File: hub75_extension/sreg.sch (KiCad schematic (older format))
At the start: 10 parts, among them U1 74HC595

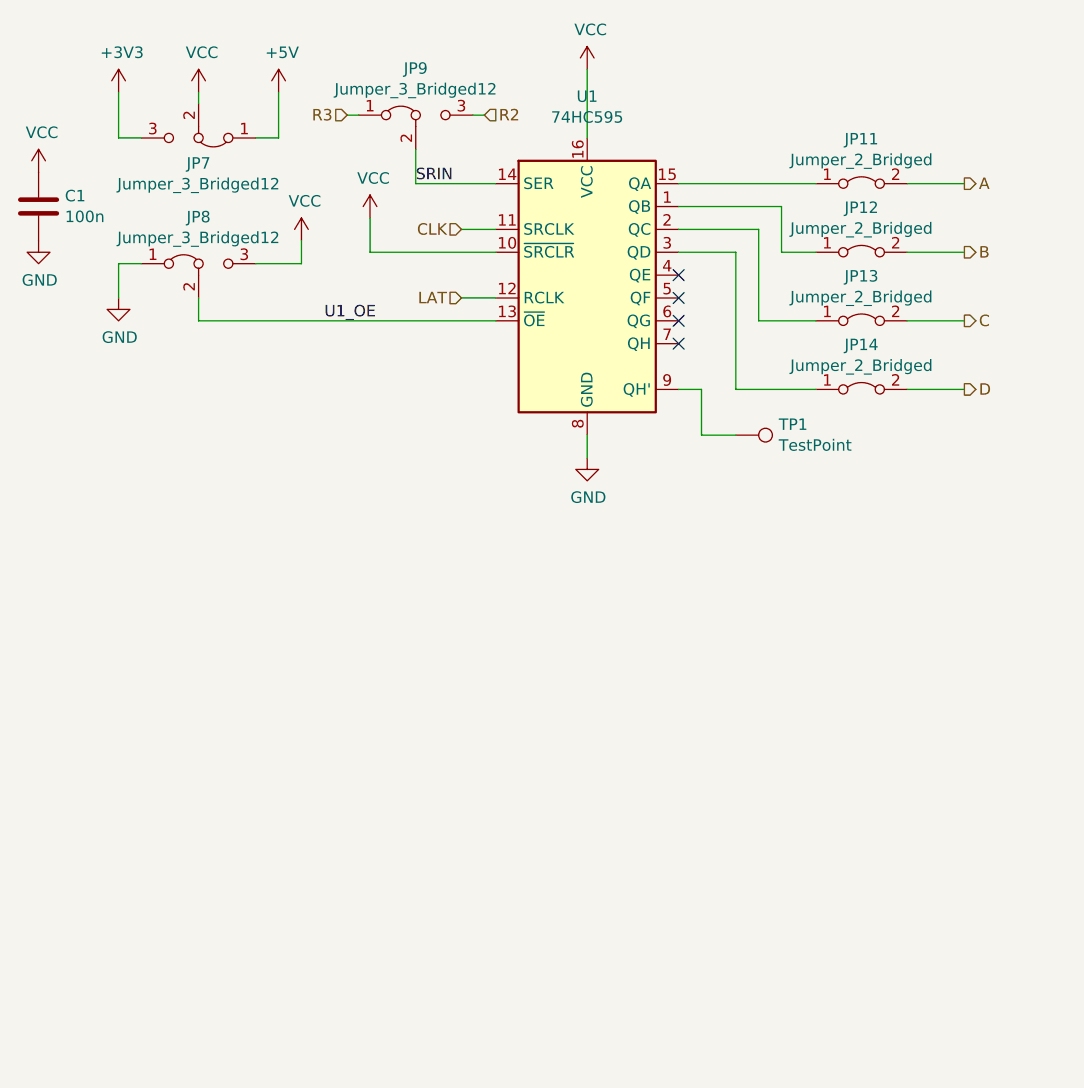
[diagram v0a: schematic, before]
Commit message: Add some spare footprints, just in case
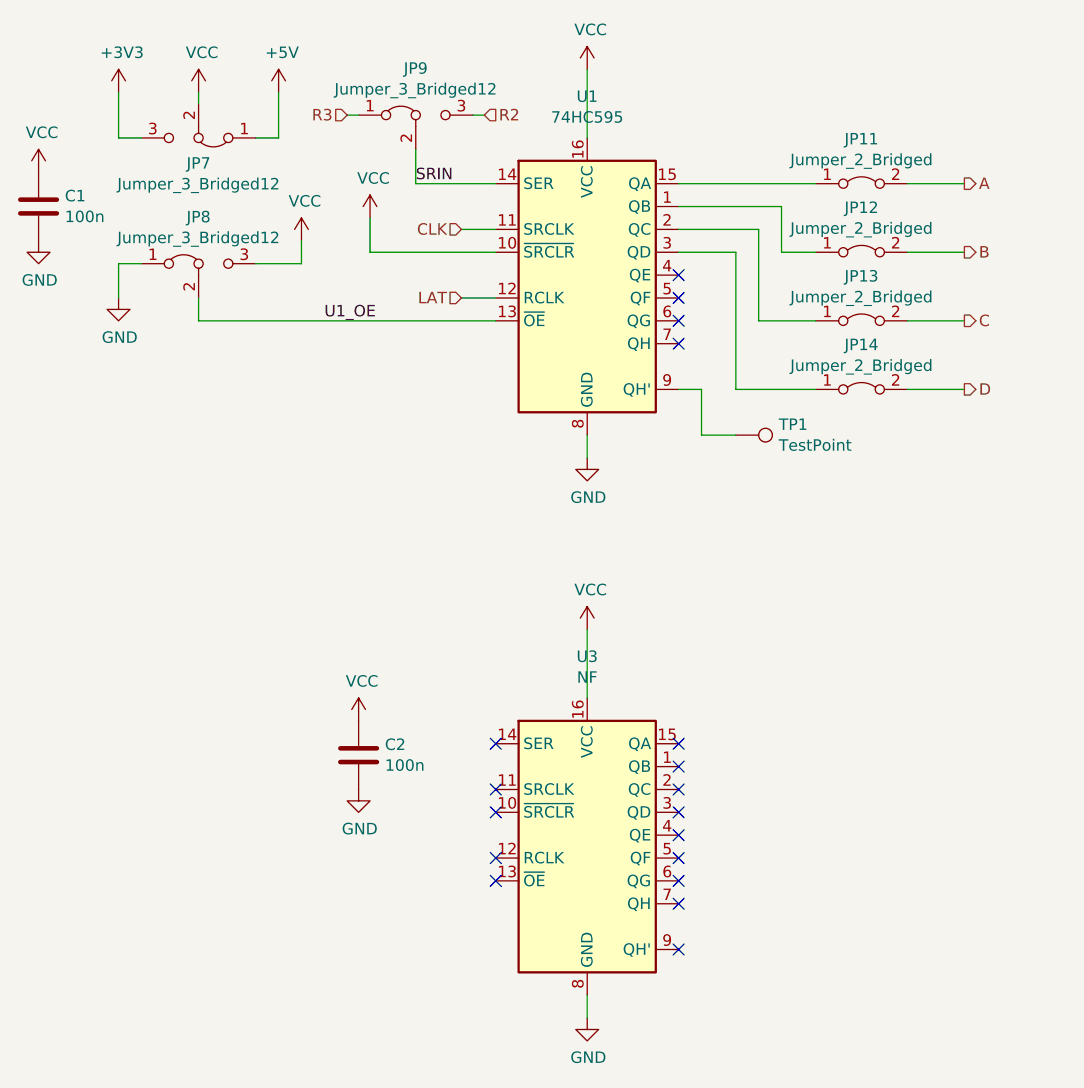
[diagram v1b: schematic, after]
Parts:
- added C2: 100n, Capacitor_SMD:C_0805_2012Metric_Pad1.18x1.45mm_HandSolder, symbol Device:C
- added U3: NF, Package_SO:SOIC-16_3.9x9.9mm_P1.27mm, symbol 74xx:74HC595
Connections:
- net GND: now also C2.2, U3.8 (GND)
- net VCC: now also C2.1, U3.16 (VCC)
- no-connect marks 4 -> 18
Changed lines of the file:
@@
 Text HLabel 5850 3400 2    50   Output ~ 0
 D
+$Comp
+L Device:C C?
+U 1 1 60842BC8
+P 3200 5000
+AR Path="/60842BC8" Ref="C?"  Part="1"
+AR Path="/602F3AD9/60842BC8" Ref="C2"  Part="1"
+F 0 "C2" H 3315 5046 50  0000 L CNN
+F 1 "100n" H 3315 4955 50  0000 L CNN
+F 2 "Capacitor_SMD:C_0805_2012Metric_Pad1.18x1.45mm_HandSolder" H 3238 4850 50  0001 C CNN
+F 3 "~" H 3200 5000 50  0001 C CNN
+F 4 "C14663" H 3200 5000 50  0001 C CNN "LCSC"
+	1    3200 5000
+	1    0    0    -1
+$EndComp
+$Comp
+L power:VCC #PWR?
+U 1 1 60842BCE
+P 3200 4850
+AR Path="/60842BCE" Ref="#PWR?"  Part="1"
+AR Path="/602F3AD9/60842BCE" Ref="#PWR052"  Part="1"
+F 0 "#PWR052" H 3200 4700 50  0001 C CNN
+F 1 "VCC" H 3215 5023 50  0000 C CNN
+F 2 "" H 3200 4850 50  0001 C CNN
+F 3 "" H 3200 4850 50  0001 C CNN
+	1    3200 4850
+	1    0    0    -1
+$EndComp
+$Comp
+L power:GND #PWR?
+U 1 1 60842BD4
+P 3200 5150
+AR Path="/60842BD4" Ref="#PWR?"  Part="1"
+AR Path="/602F3AD9/60842BD4" Ref="#PWR053"  Part="1"
+F 0 "#PWR053" H 3200 4900 50  0001 C CNN
+F 1 "GND" H 3205 4977 50  0000 C CNN
+F 2 "" H 3200 5150 50  0001 C CNN
+F 3 "" H 3200 5150 50  0001 C CNN
+	1    3200 5150
+	1    0    0    -1
+$EndComp
+$Comp
+L 74xx:74HC595 U?
+U 1 1 60847B05
+P 4200 5350
+AR Path="/60847B05" Ref="U?"  Part="1"
+AR Path="/602F3AD9/60847B05" Ref="U3"  Part="1"
+F 0 "U3" H 4200 6131 50  0000 C CNN
+F 1 "NF" H 4200 6040 50  0000 C CNN
+F 2 "Package_SO:SOIC-16_3.9x9.9mm_P1.27mm" H 4200 5350 50  0001 C CNN
+F 3 "http://www.ti.com/lit/ds/symlink/sn74hc595.pdf" H 4200 5350 50  0001 C CNN
+F 4 "C5947" H 4200 5350 50  0001 C CNN "LCSC"
+	1    4200 5350
+	1    0    0    -1
+$EndComp
+$Comp
+L power:VCC #PWR?
+U 1 1 60847B0B
+P 4200 4450
+AR Path="/60847B0B" Ref="#PWR?"  Part="1"
+AR Path="/602F3AD9/60847B0B" Ref="#PWR054"  Part="1"
+F 0 "#PWR054" H 4200 4300 50  0001 C CNN
+F 1 "VCC" H 4215 4623 50  0000 C CNN
+F 2 "" H 4200 4450 50  0001 C CNN
+F 3 "" H 4200 4450 50  0001 C CNN
+	1    4200 4450
+	1    0    0    -1
+$EndComp
+Wire Wire Line
+	4200 4450 4200 4750
+$Comp
+L power:GND #PWR?
+U 1 1 60847B12
+P 4200 6150
+AR Path="/60847B12" Ref="#PWR?"  Part="1"
+AR Path="/602F3AD9/60847B12" Ref="#PWR055"  Part="1"
+F 0 "#PWR055" H 4200 5900 50  0001 C CNN
+F 1 "GND" H 4205 5977 50  0000 C CNN
+F 2 "" H 4200 6150 50  0001 C CNN
+F 3 "" H 4200 6150 50  0001 C CNN
+	1    4200 6150
+	1    0    0    -1
+$EndComp
+Wire Wire Line
+	4200 6050 4200 6150
+NoConn ~ 3800 4950
+NoConn ~ 3800 5150
+NoConn ~ 3800 5250
+NoConn ~ 3800 5450
+NoConn ~ 3800 5550
+NoConn ~ 4600 4950
+NoConn ~ 4600 5050
+NoConn ~ 4600 5150
+NoConn ~ 4600 5250
+NoConn ~ 4600 5350
+NoConn ~ 4600 5450
+NoConn ~ 4600 5550
+NoConn ~ 4600 5650
+NoConn ~ 4600 5850
 $EndSCHEMATC

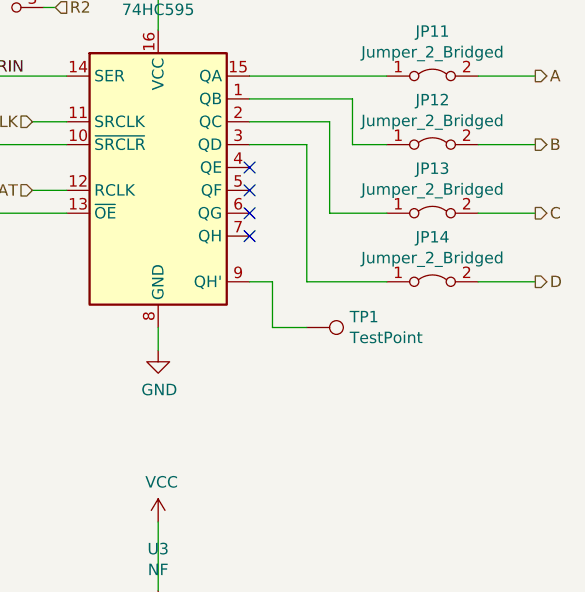
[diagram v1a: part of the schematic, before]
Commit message: Fix HUB12 Oopsie, add support for E line on HUB75
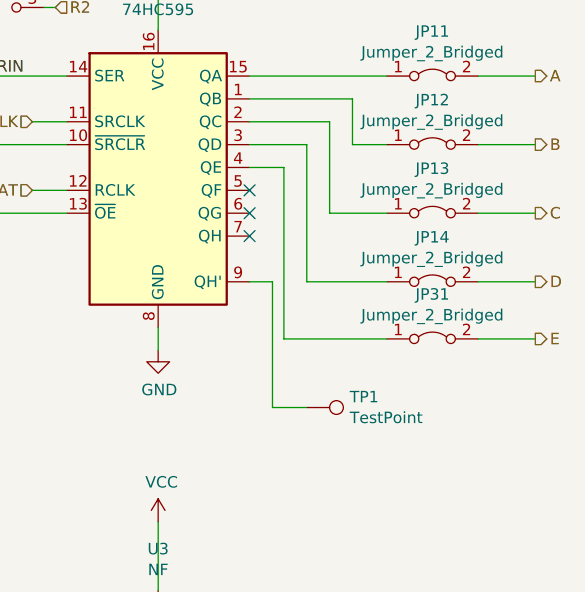
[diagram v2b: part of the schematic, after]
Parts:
- added JP31: Jumper_2_Bridged, Connector_PinHeader_2.54mm:PinHeader_1x02_P2.54mm_Vertical, symbol Jumper:Jumper_2_Bridged
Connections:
- net at U1.4 (QE): now also JP31.1 (A)
- new net E: JP31.2 (B)
- no-connect marks 18 -> 17
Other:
- moved on the sheet: TP1
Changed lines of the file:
@@
 Wire Wire Line
 	4200 2000 4200 2300
-NoConn ~ 4600 2900
 NoConn ~ 4600 3000
 NoConn ~ 4600 3100
@@
 	4600 3400 4700 3400
 Wire Wire Line
-	4700 3400 4700 3600
-Wire Wire Line
-	4700 3600 4850 3600
+	4700 3400 4700 3950
+Wire Wire Line
+	4700 3950 4850 3950
 $Comp
 L power:GND #PWR?
@@
 L Connector:TestPoint TP?
 U 1 1 60328DDF
-P 4850 3600
+P 4850 3950
 AR Path="/60328DDF" Ref="TP?"  Part="1"
 AR Path="/602F3AD9/60328DDF" Ref="TP1"  Part="1"
-F 0 "TP1" V 4804 3788 50  0000 L CNN
-F 1 "TestPoint" V 4895 3788 50  0000 L CNN
-F 2 "Connector_PinHeader_2.54mm:PinHeader_1x01_P2.54mm_Vertical" H 5050 3600 50  0001 C CNN
-F 3 "~" H 5050 3600 50  0001 C CNN
-	1    4850 3600
+F 0 "TP1" V 4804 4138 50  0000 L CNN
+F 1 "TestPoint" V 4895 4138 50  0000 L CNN
+F 2 "Connector_PinHeader_2.54mm:PinHeader_1x01_P2.54mm_Vertical" H 5050 3950 50  0001 C CNN
+F 3 "~" H 5050 3950 50  0001 C CNN
+	1    4850 3950
 	0    1    1    0
 $EndComp
@@
 NoConn ~ 4600 5650
 NoConn ~ 4600 5850
+$Comp
+L Jumper:Jumper_2_Bridged JP?
+U 1 1 609589F5
+P 5400 3650
+AR Path="/609589F5" Ref="JP?"  Part="1"
+AR Path="/602F3AD9/609589F5" Ref="JP31"  Part="1"
+F 0 "JP31" H 5400 3845 50  0000 C CNN
+F 1 "Jumper_2_Bridged" H 5400 3754 50  0000 C CNN
+F 2 "Connector_PinHeader_2.54mm:PinHeader_1x02_P2.54mm_Vertical" H 5400 3650 50  0001 C CNN
+F 3 "~" H 5400 3650 50  0001 C CNN
+	1    5400 3650
+	1    0    0    -1
+$EndComp
+Wire Wire Line
+	4600 2900 4750 2900
+Wire Wire Line
+	4750 2900 4750 3650
+Wire Wire Line
+	4750 3650 5200 3650
+Wire Wire Line
+	5600 3650 5850 3650
+Text HLabel 5850 3650 2    50   Output ~ 0
+E
 $EndSCHEMATC

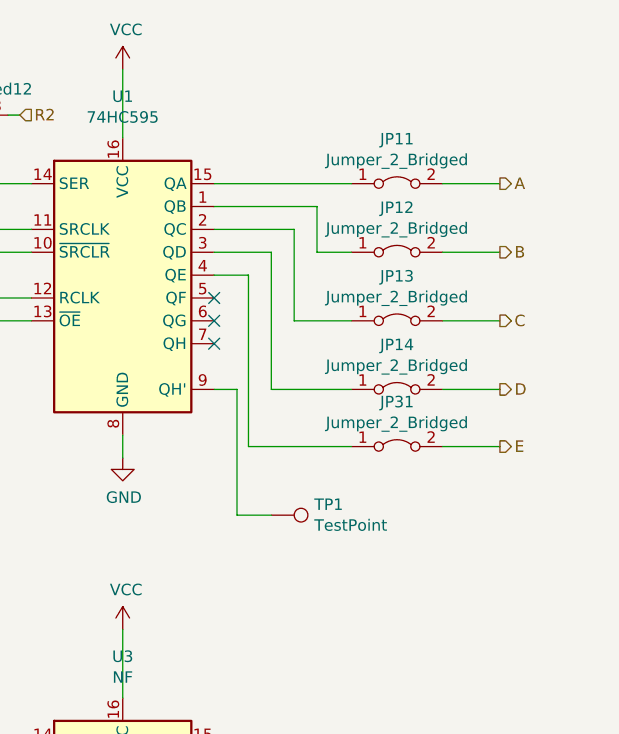
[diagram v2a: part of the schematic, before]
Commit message: Add another option for OE, coming from the sreg
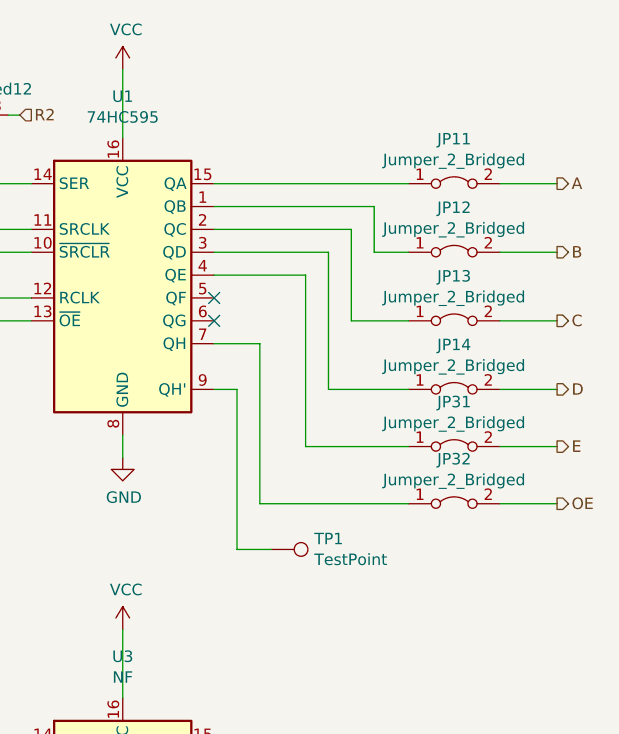
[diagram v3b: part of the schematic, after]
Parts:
- added JP32: Jumper_2_Bridged, Connector_PinHeader_2.54mm:PinHeader_1x02_P2.54mm_Vertical, symbol Jumper:Jumper_2_Bridged
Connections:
- net at U1.7 (QH): now also JP32.1 (A)
- new net OE: JP32.2 (B)
- no-connect marks 17 -> 16
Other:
- moved on the sheet: JP11, JP12, JP13, JP14, JP31, TP1
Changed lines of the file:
@@
 $EndDescr
-$Comp
-L 74xx:74HC595 U?
-U 1 1 60328D4C
-P 4200 2900
-AR Path="/60328D4C" Ref="U?"  Part="1"
-AR Path="/602F3AD9/60328D4C" Ref="U1"  Part="1"
-F 0 "U1" H 4200 3681 50  0000 C CNN
-F 1 "74HC595" H 4200 3590 50  0000 C CNN
-F 2 "Package_SO:SOIC-16_3.9x9.9mm_P1.27mm" H 4200 2900 50  0001 C CNN
-F 3 "http://www.ti.com/lit/ds/symlink/sn74hc595.pdf" H 4200 2900 50  0001 C CNN
-F 4 "C5947" H 4200 2900 50  0001 C CNN "LCSC"
-	1    4200 2900
-	1    0    0    -1
-$EndComp
 $Comp
 L Jumper:Jumper_3_Bridged12 JP?
@@
 NoConn ~ 4600 3000
 NoConn ~ 4600 3100
-NoConn ~ 4600 3200
 $Comp
 L Jumper:Jumper_2_Bridged JP?
 U 1 1 60328D98
-P 5400 2500
+P 5650 2500
 AR Path="/60328D98" Ref="JP?"  Part="1"
 AR Path="/602F3AD9/60328D98" Ref="JP11"  Part="1"
-F 0 "JP11" H 5400 2695 50  0000 C CNN
-F 1 "Jumper_2_Bridged" H 5400 2604 50  0000 C CNN
-F 2 "Connector_PinHeader_2.54mm:PinHeader_1x02_P2.54mm_Vertical" H 5400 2500 50  0001 C CNN
-F 3 "~" H 5400 2500 50  0001 C CNN
-	1    5400 2500
-	1    0    0    -1
-$EndComp
-Wire Wire Line
-	5600 2500 5850 2500
+F 0 "JP11" H 5650 2695 50  0000 C CNN
+F 1 "Jumper_2_Bridged" H 5650 2604 50  0000 C CNN
+F 2 "Connector_PinHeader_2.54mm:PinHeader_1x02_P2.54mm_Vertical" H 5650 2500 50  0001 C CNN
+F 3 "~" H 5650 2500 50  0001 C CNN
+	1    5650 2500
+	1    0    0    -1
+$EndComp
+Wire Wire Line
+	5850 2500 6100 2500
 $Comp
 L Jumper:Jumper_2_Bridged JP?
 U 1 1 60328DA0
-P 5400 2800
+P 5650 2800
 AR Path="/60328DA0" Ref="JP?"  Part="1"
 AR Path="/602F3AD9/60328DA0" Ref="JP12"  Part="1"
-F 0 "JP12" H 5400 2995 50  0000 C CNN
-F 1 "Jumper_2_Bridged" H 5400 2904 50  0000 C CNN
-F 2 "Connector_PinHeader_2.54mm:PinHeader_1x02_P2.54mm_Vertical" H 5400 2800 50  0001 C CNN
-F 3 "~" H 5400 2800 50  0001 C CNN
-	1    5400 2800
+F 0 "JP12" H 5650 2995 50  0000 C CNN
+F 1 "Jumper_2_Bridged" H 5650 2904 50  0000 C CNN
+F 2 "Connector_PinHeader_2.54mm:PinHeader_1x02_P2.54mm_Vertical" H 5650 2800 50  0001 C CNN
+F 3 "~" H 5650 2800 50  0001 C CNN
+	1    5650 2800
 	1    0    0    -1
 $EndComp
@@
 L Jumper:Jumper_2_Bridged JP?
 U 1 1 60328DA6
-P 5400 3100
+P 5650 3100
 AR Path="/60328DA6" Ref="JP?"  Part="1"
 AR Path="/602F3AD9/60328DA6" Ref="JP13"  Part="1"
-F 0 "JP13" H 5400 3295 50  0000 C CNN
-F 1 "Jumper_2_Bridged" H 5400 3204 50  0000 C CNN
-F 2 "Connector_PinHeader_2.54mm:PinHeader_1x02_P2.54mm_Vertical" H 5400 3100 50  0001 C CNN
-F 3 "~" H 5400 3100 50  0001 C CNN
-	1    5400 3100
+F 0 "JP13" H 5650 3295 50  0000 C CNN
+F 1 "Jumper_2_Bridged" H 5650 3204 50  0000 C CNN
+F 2 "Connector_PinHeader_2.54mm:PinHeader_1x02_P2.54mm_Vertical" H 5650 3100 50  0001 C CNN
+F 3 "~" H 5650 3100 50  0001 C CNN
+	1    5650 3100
 	1    0    0    -1
 $EndComp
@@
 L Jumper:Jumper_2_Bridged JP?
 U 1 1 60328DAC
-P 5400 3400
+P 5650 3400
 AR Path="/60328DAC" Ref="JP?"  Part="1"
 AR Path="/602F3AD9/60328DAC" Ref="JP14"  Part="1"
-F 0 "JP14" H 5400 3595 50  0000 C CNN
-F 1 "Jumper_2_Bridged" H 5400 3504 50  0000 C CNN
-F 2 "Connector_PinHeader_2.54mm:PinHeader_1x02_P2.54mm_Vertical" H 5400 3400 50  0001 C CNN
-F 3 "~" H 5400 3400 50  0001 C CNN
-	1    5400 3400
-	1    0    0    -1
-$EndComp
-Wire Wire Line
-	5600 2800 5850 2800
-Wire Wire Line
-	5600 3100 5850 3100
-Wire Wire Line
-	5600 3400 5850 3400
-Wire Wire Line
-	4600 2500 5200 2500
-Wire Wire Line
-	4600 2600 5050 2600
-Wire Wire Line
-	5050 2600 5050 2800
-Wire Wire Line
-	5050 2800 5200 2800
-Wire Wire Line
-	4600 2700 4950 2700
-Wire Wire Line
-	4950 2700 4950 3100
-Wire Wire Line
-	4950 3100 5200 3100
-Wire Wire Line
-	4600 2800 4850 2800
-Wire Wire Line
-	4850 2800 4850 3400
-Wire Wire Line
-	4850 3400 5200 3400
+F 0 "JP14" H 5650 3595 50  0000 C CNN
+F 1 "Jumper_2_Bridged" H 5650 3504 50  0000 C CNN
+F 2 "Connector_PinHeader_2.54mm:PinHeader_1x02_P2.54mm_Vertical" H 5650 3400 50  0001 C CNN
+F 3 "~" H 5650 3400 50  0001 C CNN
+	1    5650 3400
+	1    0    0    -1
+$EndComp
+Wire Wire Line
+	5850 2800 6100 2800
+Wire Wire Line
+	5850 3100 6100 3100
+Wire Wire Line
+	5850 3400 6100 3400
+Wire Wire Line
+	4600 2500 5450 2500
+Wire Wire Line
+	4600 2600 5300 2600
+Wire Wire Line
+	5300 2600 5300 2800
+Wire Wire Line
+	5300 2800 5450 2800
+Wire Wire Line
+	4600 2700 5200 2700
+Wire Wire Line
+	5200 2700 5200 3100
+Wire Wire Line
+	5200 3100 5450 3100
+Wire Wire Line
+	4600 2800 5100 2800
+Wire Wire Line
+	5100 2800 5100 3400
+Wire Wire Line
+	5100 3400 5450 3400
 Wire Wire Line
 	4600 3400 4700 3400
 Wire Wire Line
-	4700 3400 4700 3950
-Wire Wire Line
-	4700 3950 4850 3950
+	4700 3400 4700 4100
+Wire Wire Line
+	4700 4100 4850 4100
 $Comp
 L power:GND #PWR?
@@
 L Connector:TestPoint TP?
 U 1 1 60328DDF
-P 4850 3950
+P 4850 4100
 AR Path="/60328DDF" Ref="TP?"  Part="1"
 AR Path="/602F3AD9/60328DDF" Ref="TP1"  Part="1"
-F 0 "TP1" V 4804 4138 50  0000 L CNN
-F 1 "TestPoint" V 4895 4138 50  0000 L CNN
-F 2 "Connector_PinHeader_2.54mm:PinHeader_1x01_P2.54mm_Vertical" H 5050 3950 50  0001 C CNN
-F 3 "~" H 5050 3950 50  0001 C CNN
-	1    4850 3950
+F 0 "TP1" V 4804 4288 50  0000 L CNN
+F 1 "TestPoint" V 4895 4288 50  0000 L CNN
+F 2 "Connector_PinHeader_2.54mm:PinHeader_1x01_P2.54mm_Vertical" H 5050 4100 50  0001 C CNN
+F 3 "~" H 5050 4100 50  0001 C CNN
+	1    4850 4100
 	0    1    1    0
 $EndComp
@@
 Text HLabel 3650 3000 0    50   Input ~ 0
 LAT
-Text HLabel 5850 2500 2    50   Output ~ 0
+Text HLabel 6100 2500 2    50   Output ~ 0
 A
-Text HLabel 5850 2800 2    50   Output ~ 0
+Text HLabel 6100 2800 2    50   Output ~ 0
 B
-Text HLabel 5850 3100 2    50   Output ~ 0
+Text HLabel 6100 3100 2    50   Output ~ 0
 C
-Text HLabel 5850 3400 2    50   Output ~ 0
+Text HLabel 6100 3400 2    50   Output ~ 0
 D
 $Comp
@@
 L Jumper:Jumper_2_Bridged JP?
 U 1 1 609589F5
-P 5400 3650
+P 5650 3650
 AR Path="/609589F5" Ref="JP?"  Part="1"
 AR Path="/602F3AD9/609589F5" Ref="JP31"  Part="1"
-F 0 "JP31" H 5400 3845 50  0000 C CNN
-F 1 "Jumper_2_Bridged" H 5400 3754 50  0000 C CNN
-F 2 "Connector_PinHeader_2.54mm:PinHeader_1x02_P2.54mm_Vertical" H 5400 3650 50  0001 C CNN
-F 3 "~" H 5400 3650 50  0001 C CNN
-	1    5400 3650
-	1    0    0    -1
-$EndComp
-Wire Wire Line
-	4600 2900 4750 2900
-Wire Wire Line
-	4750 2900 4750 3650
-Wire Wire Line
-	4750 3650 5200 3650
-Wire Wire Line
-	5600 3650 5850 3650
-Text HLabel 5850 3650 2    50   Output ~ 0
+F 0 "JP31" H 5650 3845 50  0000 C CNN
+F 1 "Jumper_2_Bridged" H 5650 3754 50  0000 C CNN
+F 2 "Connector_PinHeader_2.54mm:PinHeader_1x02_P2.54mm_Vertical" H 5650 3650 50  0001 C CNN
+F 3 "~" H 5650 3650 50  0001 C CNN
+	1    5650 3650
+	1    0    0    -1
+$EndComp
+Wire Wire Line
+	4600 2900 5000 2900
+Wire Wire Line
+	5000 2900 5000 3650
+Wire Wire Line
+	5000 3650 5450 3650
+Wire Wire Line
+	5850 3650 6100 3650
+Text HLabel 6100 3650 2    50   Output ~ 0
 E
+$Comp
+L Jumper:Jumper_2_Bridged JP?
+U 1 1 609A10D5
+P 5650 3900
+AR Path="/609A10D5" Ref="JP?"  Part="1"
+AR Path="/602F3AD9/609A10D5" Ref="JP32"  Part="1"
+F 0 "JP32" H 5650 4095 50  0000 C CNN
+F 1 "Jumper_2_Bridged" H 5650 4004 50  0000 C CNN
+F 2 "Connector_PinHeader_2.54mm:PinHeader_1x02_P2.54mm_Vertical" H 5650 3900 50  0001 C CNN
+F 3 "~" H 5650 3900 50  0001 C CNN
+	1    5650 3900
+	1    0    0    -1
+$EndComp
+$Comp
+L 74xx:74HC595 U?
+U 1 1 60328D4C
+P 4200 2900
+AR Path="/60328D4C" Ref="U?"  Part="1"
+AR Path="/602F3AD9/60328D4C" Ref="U1"  Part="1"
+F 0 "U1" H 4200 3681 50  0000 C CNN
+F 1 "74HC595" H 4200 3590 50  0000 C CNN
+F 2 "Package_SO:SOIC-16_3.9x9.9mm_P1.27mm" H 4200 2900 50  0001 C CNN
+F 3 "http://www.ti.com/lit/ds/symlink/sn74hc595.pdf" H 4200 2900 50  0001 C CNN
+F 4 "C5947" H 4200 2900 50  0001 C CNN "LCSC"
+	1    4200 2900
+	1    0    0    -1
+$EndComp
+Wire Wire Line
+	4600 3200 4800 3200
+Wire Wire Line
+	4800 3200 4800 3900
+Wire Wire Line
+	4800 3900 5450 3900
+Text HLabel 6100 3900 2    50   Output ~ 0
+OE
+Wire Wire Line
+	5850 3900 6100 3900
 $EndSCHEMATC
